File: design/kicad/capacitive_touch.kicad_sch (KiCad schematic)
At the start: 66 parts, among them J15 Conn_01x12_Socket, J16 Conn_01x12_Pin, J2 Conn_01x09_Pin, J5 Conn_01x12_Socket, J6 Conn_01x12_Socket, J7 Conn_01x12_Socket, J8 Conn_01x09_Pin, J9 Conn_01x09_Pin, U10 MPR121QR2, U4 MPR121QR2, U5 MPR121QR2, U6 MPR121QR2

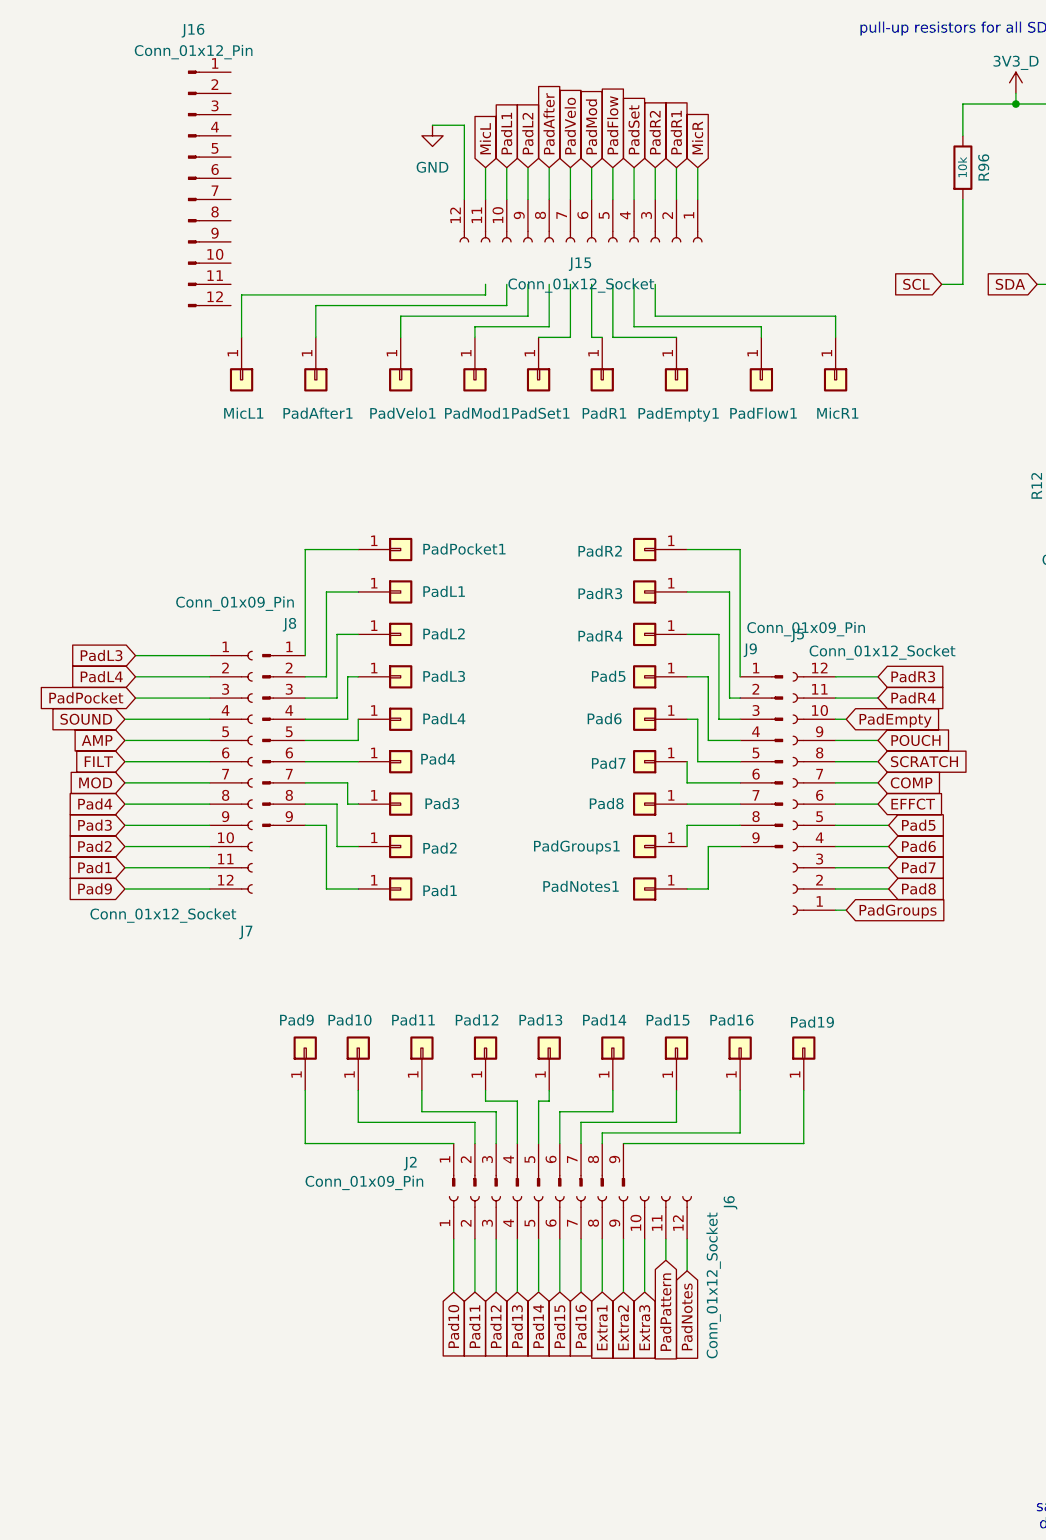
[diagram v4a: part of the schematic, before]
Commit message: PCB all routed, Moves top components to top file
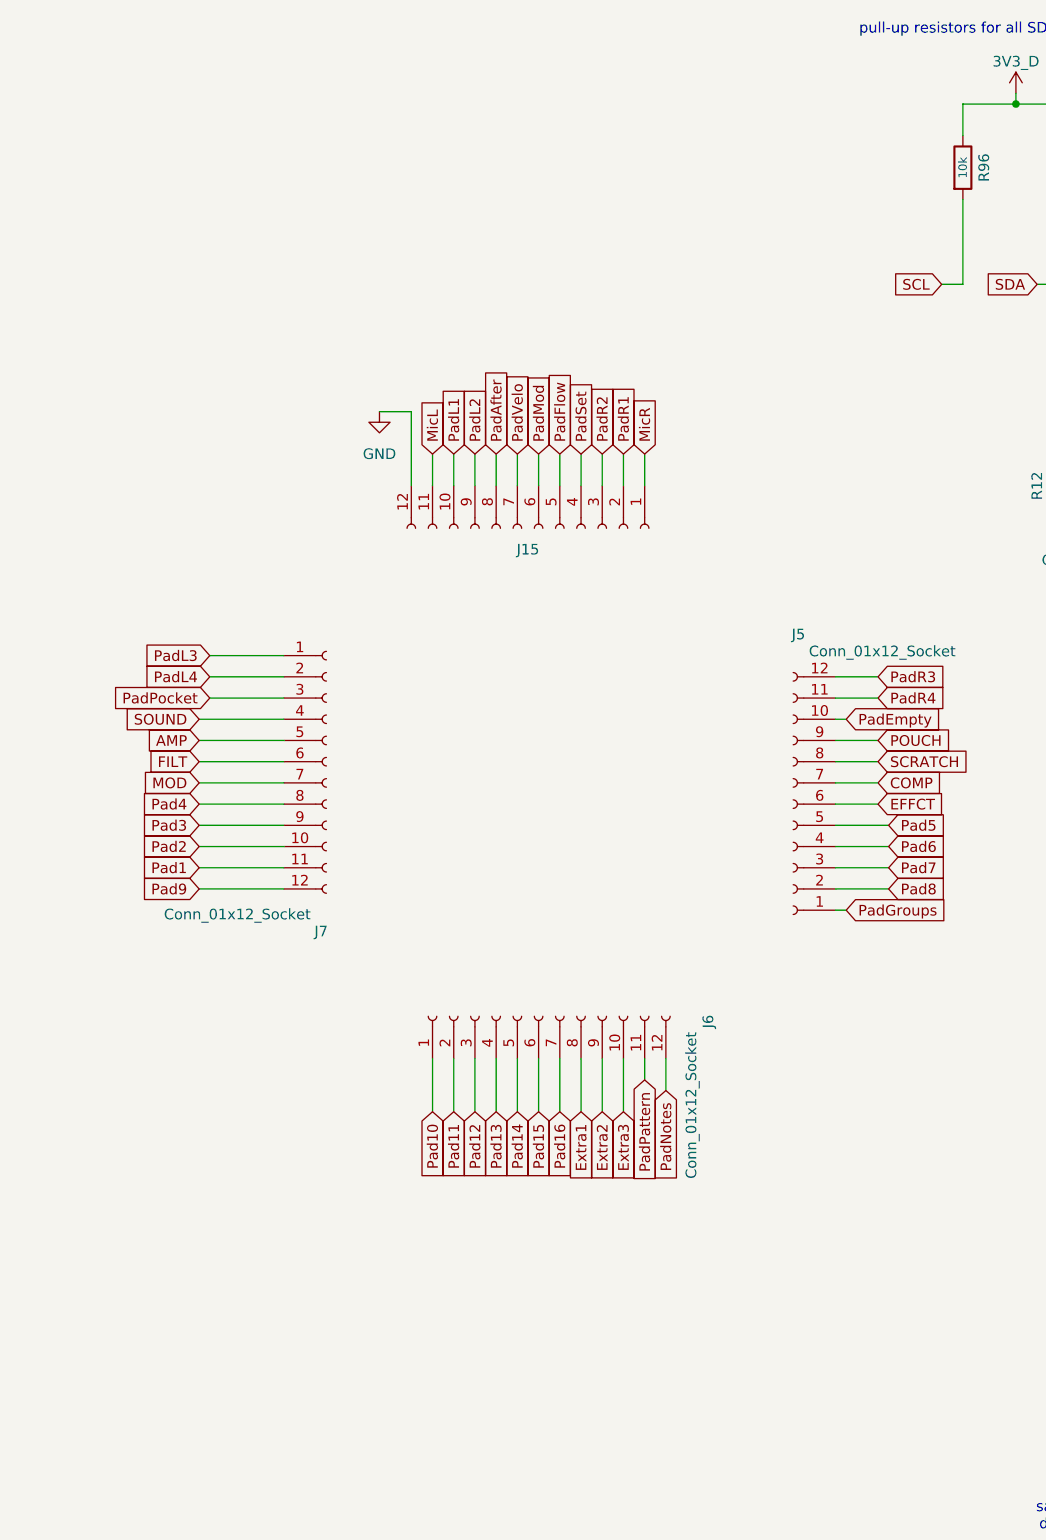
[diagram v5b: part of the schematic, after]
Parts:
- removed J16: Conn_01x12_Pin, Connector_PinHeader_1.27mm:PinHeader_1x12_P1.27mm_Vertical_SMD_Pin1Left, symbol Connector:Conn_01x12_Pin
- removed J2, J8, J9: Conn_01x09_Pin, Connector_PinHeader_1.27mm:PinHeader_1x09_P1.27mm_Vertical_SMD_Pin1Left, symbol Connector:Conn_01x09_Pin
- removed MicL1, MicR1, Pad1, Pad10, Pad11, Pad12, Pad13, Pad14, Pad15, Pad16, Pad19, Pad2, Pad3, Pad4, Pad5, Pad6, Pad7, Pad8, Pad9, PadAfter1, PadEmpty1, PadFlow1, PadGroups1, PadL1, PadL2, PadL3, PadL4, PadMod1, PadNotes1, PadPocket1, PadR1, PadR2, PadR3, PadR4, PadSet1, PadVelo1: Conn_01x01, TestPoint:TestPoint_Pad_2.5x2.5mm, symbol Connector_Generic:Conn_01x01
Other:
- moved on the sheet: J15, J6, J7

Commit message: shortens SD data lines
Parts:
- R12, R16, R20, R91: footprint Resistor_SMD:R_0603_1608Metric -> Resistor_SMD:R_0402_1005Metric; LCSC C2907088 -> C25741
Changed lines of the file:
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@@
 			)
 		)
-		(property "Footprint" "Resistor_SMD:R_0603_1608Metric"
+		(property "Footprint" "Resistor_SMD:R_0402_1005Metric"
 			(at 133.858 69.85 90)
 			(effects
@@
 			)
 		)
-		(property "LCSC" " C2907088"
+		(property "LCSC" "C25741"
 			(at 132.08 69.85 90)
 			(effects
@@
 			)
 		)
-		(property "Footprint" "Resistor_SMD:R_0603_1608Metric"
+		(property "Footprint" "Resistor_SMD:R_0402_1005Metric"
 			(at 138.938 143.51 90)
 			(effects
@@
 			)
 		)
-		(property "LCSC" " C2907088"
+		(property "LCSC" "C25741"
 			(at 137.16 143.51 90)
 			(effects
@@
 			)
 		)
-		(property "Footprint" "Resistor_SMD:R_0603_1608Metric"
+		(property "Footprint" "Resistor_SMD:R_0402_1005Metric"
 			(at 213.868 143.51 90)
 			(effects
@@
 			)
 		)
-		(property "LCSC" " C2907088"
+		(property "LCSC" "C25741"
 			(at 212.09 143.51 0)
 			(effects
@@
 			)
 		)
-		(property "Footprint" "Resistor_SMD:R_0603_1608Metric"
+		(property "Footprint" "Resistor_SMD:R_0402_1005Metric"
 			(at 212.598 72.39 90)
 			(effects
@@
 			)
 		)
-		(property "LCSC" " C2907088"
+		(property "LCSC" "C25741"
 			(at 210.82 72.39 0)
 			(effects

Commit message: pcb rules fixes, reroute suggestions
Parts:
- removed R16, R20, R91: 100k, Resistor_SMD:R_0402_1005Metric, symbol Device:R
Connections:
- net 3V3_D: now also U5.4 (ADDR)
- net SCL: now also U10.4 (ADDR)
- net SDA: now also U6.4 (ADDR)

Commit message: last commit before refactor repo: kicad mostly
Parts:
- removed C15, C16, C4, C5, C6, C7, C8, C9: 0.1uF, Capacitor_SMD:C_0402_1005Metric, symbol Device:C
- removed J15, J5, J6, J7: Conn_01x12_Socket, Connector_PinSocket_1.27mm:PinSocket_1x12_P1.27mm_Vertical, symbol Connector:Conn_01x12_Socket
- removed R11, R18, R22, R93: 75k, Resistor_SMD:R_0603_1608Metric, symbol Device:R
- removed R12: 100k, Resistor_SMD:R_0402_1005Metric, symbol Device:R
- removed R96, R99: 10k, Resistor_SMD:R_0603_1608Metric, symbol Device:R
- removed U10, U4, U5, U6: MPR121QR2, Package_DFN_QFN:UQFN-20_3x3mm_P0.4mm, symbol Sensor_Touch:MPR121QR2
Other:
- note removed: "pull-up resistors for all SDA and SCL lines"
